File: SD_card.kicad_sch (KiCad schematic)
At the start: 6 parts, among them J13 TF-15x15

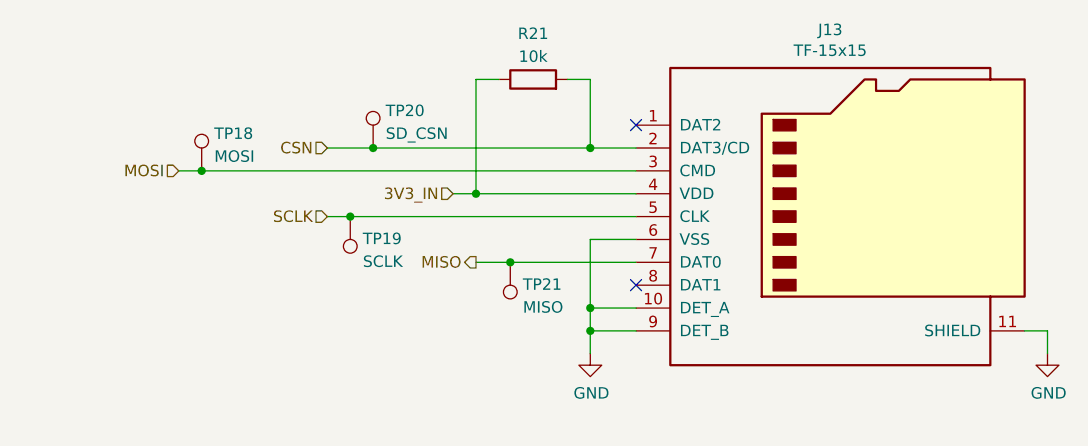
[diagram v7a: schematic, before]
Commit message: Add 5V boost converter and begin redesign of PCB
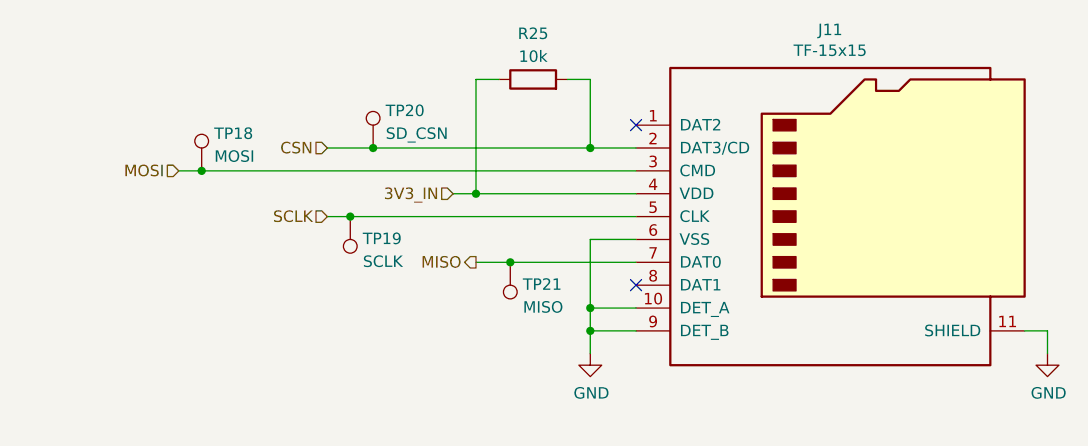
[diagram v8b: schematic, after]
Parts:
- renumbered J13 to J11, R21 to R25
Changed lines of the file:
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@@
   (symbol (lib_id "power:GND") (at 137.16 111.76 0) (unit 1)
     (in_bom yes) (on_board yes)
-    (property "Reference" "#PWR052" (id 0) (at 137.16 118.11 0)
+    (property "Reference" "#PWR065" (id 0) (at 137.16 118.11 0)
       (effects (font (size 1.27 1.27)) hide)
     )
@@
   (symbol (lib_id "power:GND") (at 187.96 111.76 0) (unit 1)
     (in_bom yes) (on_board yes)
-    (property "Reference" "#PWR053" (id 0) (at 187.96 118.11 0)
+    (property "Reference" "#PWR066" (id 0) (at 187.96 118.11 0)
       (effects (font (size 1.27 1.27)) hide)
     )
@@
   (symbol (lib_id "Connector:Micro_SD_Card_Det") (at 165.1 96.52 0) (unit 1)
     (in_bom yes) (on_board yes)
-    (property "Reference" "J13" (id 0) (at 163.83 75.7682 0))
+    (property "Reference" "J11" (id 0) (at 163.83 75.7682 0))
     (property "Value" "TF-15x15" (id 1) (at 163.83 78.0796 0))
     (property "Footprint" "co2_sensor_node:TF-15x15" (id 2) (at 217.17 78.74 0)
@@
   (symbol (lib_id "Device:R") (at 130.81 81.28 90) (unit 1)
     (in_bom yes) (on_board yes)
-    (property "Reference" "R21" (id 0) (at 130.81 76.2 90))
+    (property "Reference" "R25" (id 0) (at 130.81 76.2 90))
     (property "Value" "10k" (id 1) (at 130.81 78.74 90))
     (property "Footprint" "Resistor_SMD:R_0603_1608Metric" (id 2) (at 130.81 83.058 90)
